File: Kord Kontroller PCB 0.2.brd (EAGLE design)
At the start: 242.5 x 100 mm, 190 parts, among them IC2 74HCT1G125DBV, J1 MIDIOUTB, J2 MIDIOUTA, J3 FTSH-105-01-L-DV-KJ, SW2 SPST_TACT-KMR2, U1 AP2112K-3.3, U2 ATSAMD51J19A-AUT, X3 microUSB

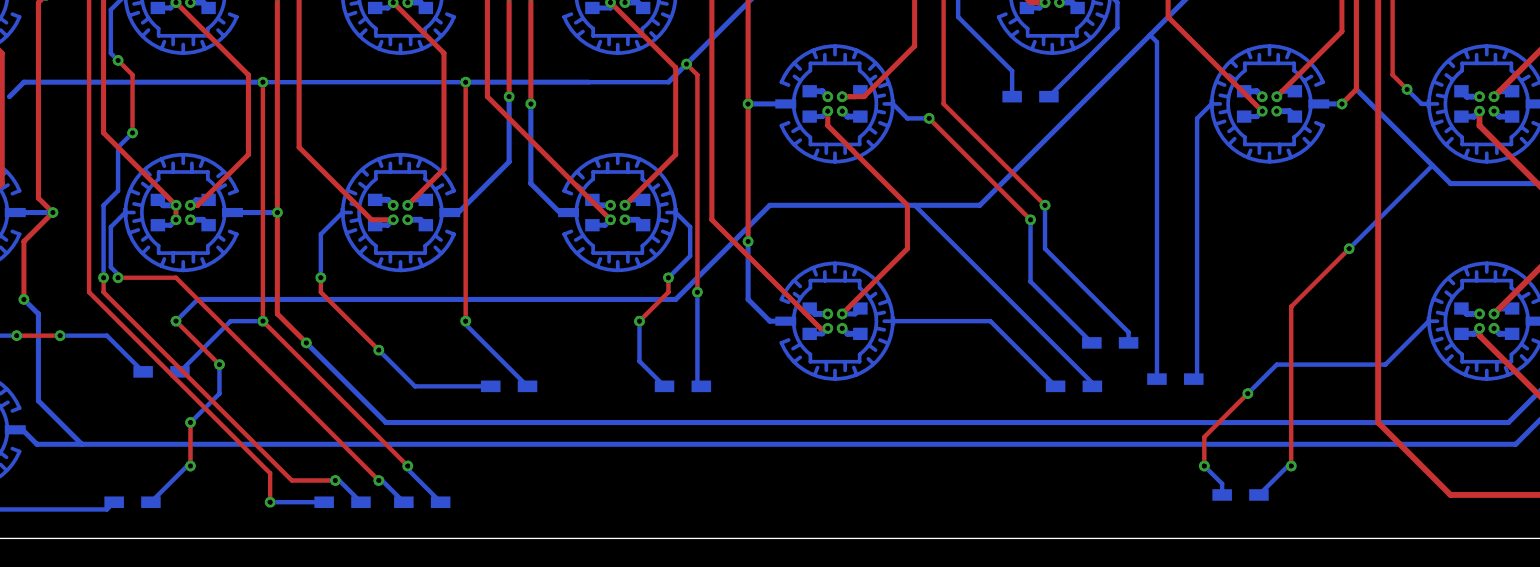
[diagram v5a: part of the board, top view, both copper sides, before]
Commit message: Minor resistor change
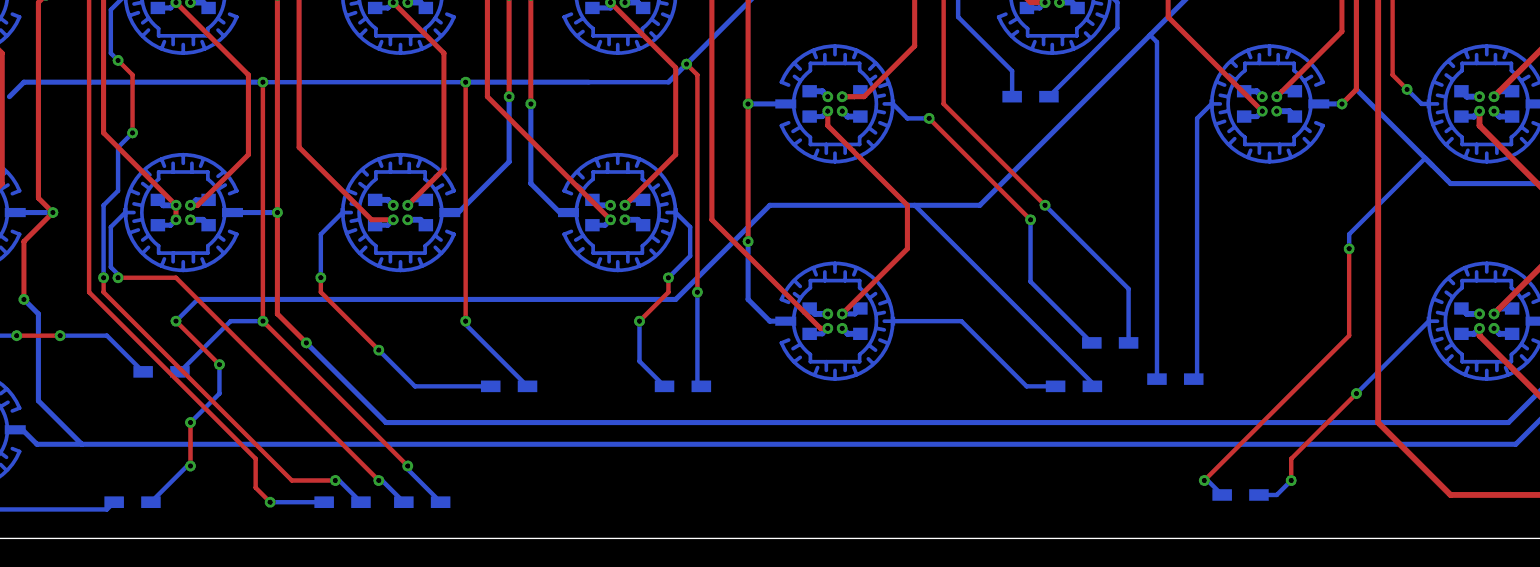
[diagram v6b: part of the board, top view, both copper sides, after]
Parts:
- turned D28 to 0 degrees
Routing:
- net N$131: track 23.3 -> 17.6 mm
- net ROW4: track 256.5 -> 261.0 mm
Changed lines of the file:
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@@
 <setting verticaltext="up"/>
 </settings>
-<grid distance="7.5" unitdist="mm" unit="mm" style="lines" multiple="1" display="yes" altdistance="1" altunitdist="mm" altunit="mm"/>
+<grid distance="1" unitdist="mm" unit="mm" style="lines" multiple="1" display="yes" altdistance="1" altunitdist="mm" altunit="mm"/>
 <layers>
 <layer number="1" name="Top" color="4" fill="1" visible="yes" active="yes"/>
@@
 <element name="B49" library="microbuilder" package="ELAST_PAD_SQUARE_10MM_4X4WIDE" value="ELAST_10X10" x="22.5" y="22.5" smashed="yes" rot="MR0"/>
 <element name="B53" library="microbuilder" package="ELAST_PAD_SQUARE_10MM_4X4WIDE" value="ELAST_10X10" x="7.5" y="22.5" smashed="yes" rot="MR0"/>
-<element name="D28" library="microbuilder" package="SOD-323" value="1N4148" x="95.5" y="3" smashed="yes" rot="MR180">
-<attribute name="NAME" x="94.4" y="2" size="0.8128" layer="26" ratio="18" rot="MR180"/>
-<attribute name="VALUE" x="94.4" y="4.792" size="0.4064" layer="28" ratio="10" rot="MR180"/>
+<element name="D28" library="microbuilder" package="SOD-323" value="1N4148" x="95.5" y="3" smashed="yes" rot="MR0">
+<attribute name="NAME" x="96.6" y="4" size="0.8128" layer="26" ratio="18" rot="MR0"/>
+<attribute name="VALUE" x="96.6" y="1.208" size="0.4064" layer="28" ratio="10" rot="MR0"/>
 </element>
 <element name="D32" library="microbuilder" package="SOD-323" value="1N4148" x="91" y="11" smashed="yes" rot="MR0">
@@
 <wire x1="15" y1="46.5" x2="15" y2="47.5" width="0.3048" layer="1"/>
 <via x="15" y="47.5" extent="1-16" drill="0.35"/>
-<wire x1="28.5" y1="4.5" x2="28.5" y2="2.5" width="0.3048" layer="1"/>
-<wire x1="28.5" y1="4.5" x2="16" y2="17" width="0.3048" layer="1"/>
+<wire x1="27.5" y1="5.5" x2="27.5" y2="3.5" width="0.3048" layer="1"/>
+<wire x1="27.5" y1="3.5" x2="28.5" y2="2.5" width="0.3048" layer="1"/>
+<wire x1="27.5" y1="5.5" x2="16" y2="17" width="0.3048" layer="1"/>
 <via x="28.5" y="2.5" extent="1-16" drill="0.35"/>
 <wire x1="17.27" y1="79.5" x2="17.27" y2="74.27" width="0.3048" layer="16"/>
@@
 <wire x1="79.73" y1="30.5" x2="79.73" y2="32.27" width="0.3048" layer="16"/>
 <wire x1="79.73" y1="32.27" x2="76" y2="36" width="0.3048" layer="16"/>
-<wire x1="87.77" y1="13.5" x2="87.77" y2="14.23" width="0.3048" layer="16"/>
-<wire x1="87.77" y1="14.23" x2="82" y2="20" width="0.3048" layer="16"/>
-<wire x1="82" y1="20" x2="82" y2="23" width="0.3048" layer="16"/>
+<wire x1="87.77" y1="13.5" x2="87.77" y2="17.23" width="0.3048" layer="16"/>
+<wire x1="87.77" y1="17.23" x2="82" y2="23" width="0.3048" layer="16"/>
 <via x="82" y="23" extent="1-16" drill="0.35"/>
 <wire x1="82" y1="23" x2="75" y2="30" width="0.3048" layer="1"/>
@@
 <wire x1="122.5" y1="35" x2="122.5" y2="26.5" width="0.35" layer="1"/>
 <via x="122.5" y="26.5" extent="1-16" drill="0.35"/>
-<wire x1="110" y1="24.5" x2="108.75" y2="25.75" width="0.35" layer="16"/>
-<wire x1="108.75" y1="25.75" x2="103.5" y2="31" width="0.35" layer="16"/>
+<wire x1="110" y1="24.5" x2="109.75" y2="24.75" width="0.35" layer="16"/>
+<wire x1="109.75" y1="24.75" x2="108.25" y2="26.25" width="0.35" layer="16"/>
+<wire x1="103.5" y1="31" x2="108.75" y2="25.75" width="0.35" layer="16"/>
 <wire x1="77.5" y1="23" x2="73" y2="23" width="0.35" layer="16"/>
 <wire x1="73" y1="23" x2="63" y2="23" width="0.35" layer="16"/>
@@
 <via x="122.5" y="19" extent="1-16" drill="0.35"/>
 <wire x1="140" y1="5" x2="126" y2="19" width="0.3048" layer="16"/>
-<wire x1="96.77" y1="3" x2="98.77" y2="5" width="0.3048" layer="16"/>
-<wire x1="98.77" y1="5" x2="99" y2="5" width="0.3048" layer="16"/>
-<via x="99" y="5" extent="1-16" drill="0.35"/>
-<wire x1="99" y1="16" x2="103" y2="20" width="0.3048" layer="1"/>
-<wire x1="99" y1="16" x2="99" y2="5" width="0.3048" layer="1"/>
+<wire x1="94.23" y1="3" x2="93.23" y2="4" width="0.3048" layer="16"/>
+<wire x1="93.23" y1="4" x2="93" y2="4" width="0.3048" layer="16"/>
+<via x="93" y="4" extent="1-16" drill="0.35"/>
+<wire x1="103" y1="14" x2="103" y2="20" width="0.3048" layer="1"/>
+<wire x1="103" y1="14" x2="93" y2="4" width="0.3048" layer="1"/>
 <via x="103" y="20" extent="1-16" drill="0.35"/>
-<wire x1="103" y1="20" x2="108.75" y2="25.75" width="0.3048" layer="16"/>
+<wire x1="108.25" y1="26.25" x2="103" y2="21" width="0.3048" layer="16"/>
+<wire x1="103" y1="20" x2="103" y2="21" width="0.3048" layer="16"/>
 <wire x1="103.5" y1="39" x2="93.5" y2="39" width="0.3048" layer="16"/>
 <wire x1="89.73" y1="11" x2="89.73" y2="34.27" width="0.3048" layer="16"/>
@@
 <via x="22" y="15" extent="1-16" drill="0.35"/>
 <wire x1="22" y1="15" x2="23.5" y2="16.5" width="0.3048" layer="16"/>
+<wire x1="108.75" y1="25.75" x2="109.75" y2="24.75" width="0.3048" layer="16"/>
 </signal>
 <signal name="N$110">
@@
 <contactref element="D28" pad="C"/>
 <contactref element="B28" pad="P$2"/>
-<wire x1="108.5" y1="15" x2="105.5" y2="12" width="0.3048" layer="16"/>
-<wire x1="105.5" y1="12" x2="98" y2="12" width="0.3048" layer="16"/>
-<wire x1="98" y1="12" x2="96" y2="10" width="0.3048" layer="16"/>
-<via x="96" y="10" extent="1-16" drill="0.35"/>
-<wire x1="96" y1="10" x2="93" y2="7" width="0.3048" layer="1"/>
-<wire x1="93" y1="7" x2="93" y2="5" width="0.3048" layer="1"/>
-<via x="93" y="5" extent="1-16" drill="0.35"/>
-<wire x1="93" y1="5" x2="94.23" y2="3.77" width="0.3048" layer="16"/>
-<wire x1="94.23" y1="3.77" x2="94.23" y2="3" width="0.3048" layer="16"/>
+<wire x1="108.5" y1="15" x2="103.5" y2="10" width="0.3048" layer="16"/>
+<via x="103.5" y="10" extent="1-16" drill="0.35"/>
+<wire x1="103.5" y1="10" x2="99" y2="5.5" width="0.3048" layer="1"/>
+<wire x1="99" y1="4" x2="99" y2="5.5" width="0.3048" layer="1"/>
+<via x="99" y="4" extent="1-16" drill="0.35"/>
+<wire x1="99" y1="4" x2="98" y2="3" width="0.3048" layer="16"/>
+<wire x1="96.77" y1="3" x2="98" y2="3" width="0.3048" layer="16"/>
 </signal>
 <signal name="N$132">
@@
 <contactref element="D39" pad="C"/>
 <contactref element="B39" pad="P$2"/>
-<wire x1="82.73" y1="10.5" x2="78.23" y2="15" width="0.3048" layer="16"/>
-<wire x1="78.23" y1="15" x2="71.5" y2="15" width="0.3048" layer="16"/>
+<wire x1="82.73" y1="10.5" x2="80.73" y2="10.5" width="0.3048" layer="16"/>
+<wire x1="80.73" y1="10.5" x2="76.23" y2="15" width="0.3048" layer="16"/>
+<wire x1="76.23" y1="15" x2="71.5" y2="15" width="0.3048" layer="16"/>
 </signal>
 <signal name="N$138">

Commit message: moved some stuff around
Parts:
- Q1: value (none) -> 32kHz
- moved D5 2.24 mm to (217.4, 63.9)
- moved D15 2.00 mm to (173.7, 76.5)
- moved D4 1.41 mm to (220.4, 66.4)
- moved D11 1.00 mm to (184.2, 76.9)
- moved D16 1.00 mm to (179.4, 77.0)
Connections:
- net AVDD renamed VDDANA
- removed net INT: U2.16
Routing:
- net ROW4: track 261.0 -> 254.2 mm
- net GND: track 139.3 -> 145.3 mm, vias 79 -> 81
- net ROW2: track 669.5 -> 672.8 mm
- net ROW3: track 634.2 -> 632.2 mm
- net N$48: track 11.8 -> 9.95 mm
- net N$2: track 6.42 -> 8.18 mm
- net N$59: track 39.6 -> 40.8 mm
- net COL13: track 189.9 -> 191.0 mm
- net COL7: track 95.0 -> 96.1 mm
- net SWDCLK: track 61.5 -> 60.5 mm
- net N$52: track 38.1 -> 37.1 mm
- net ROW1: track 440.5 -> 439.6 mm, vias 10 -> 8
- net N$5: track 12.0 -> 11.2 mm
- net ROW0: track 250.3 -> 249.6 mm
- net MIDIOUTA: track 143.8 -> 143.1 mm
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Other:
- board text added: "Rev-A"

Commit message: Rotated LEDs to remove DRC errors
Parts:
- turned LED1 to 270 degrees
- turned LED10 to 270 degrees
- turned LED11 to 270 degrees
- turned LED12 to 270 degrees
- turned LED13 to 270 degrees
- turned LED14 to 270 degrees
- turned LED15 to 270 degrees
- turned LED16 to 270 degrees
- turned LED17 to 270 degrees
- turned LED18 to 270 degrees
- turned LED19 to 270 degrees
- turned LED2 to 270 degrees
- turned LED20 to 270 degrees
- turned LED21 to 270 degrees
- turned LED22 to 270 degrees
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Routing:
- net N$8: track 47.8 -> 77.2 mm, vias 2 -> 4
- net ROW3: track 632.2 -> 614.3 mm
- net N$103: track 56.1 -> 73.4 mm
- net N$113: track 47.6 -> 64.2 mm
- net GND: track 145.3 -> 129.3 mm, vias 81 -> 78
- net N$100: track 60.2 -> 75.5 mm
- net N$45: track 83.9 -> 98.9 mm, vias 2 -> 4
- net N$17: track 59.4 -> 73.5 mm, vias 2 -> 4
- net N$34: track 63.0 -> 76.1 mm
- net N$37: track 48.1 -> 60.7 mm
- net N$13: track 41.1 -> 53.6 mm, vias 2 -> 4
- net N$95: track 48.0 -> 59.5 mm
- net N$50: track 33.3 -> 44.1 mm
- net N$40: track 56.9 -> 67.4 mm
- net N$59: track 40.8 -> 51.2 mm
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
